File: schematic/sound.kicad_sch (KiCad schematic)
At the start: 14 parts, among them J2 Conn_01x02, U1 LM386, U2 SN76489AN

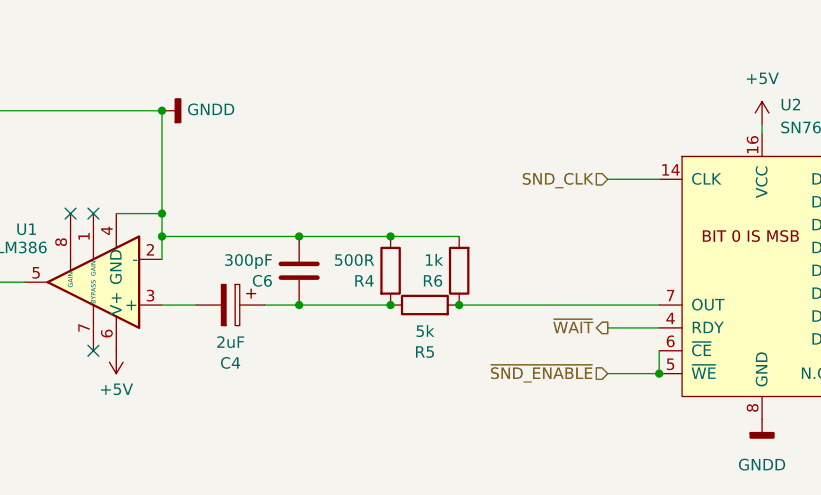
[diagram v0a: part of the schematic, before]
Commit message: added volume and adjusted cart port
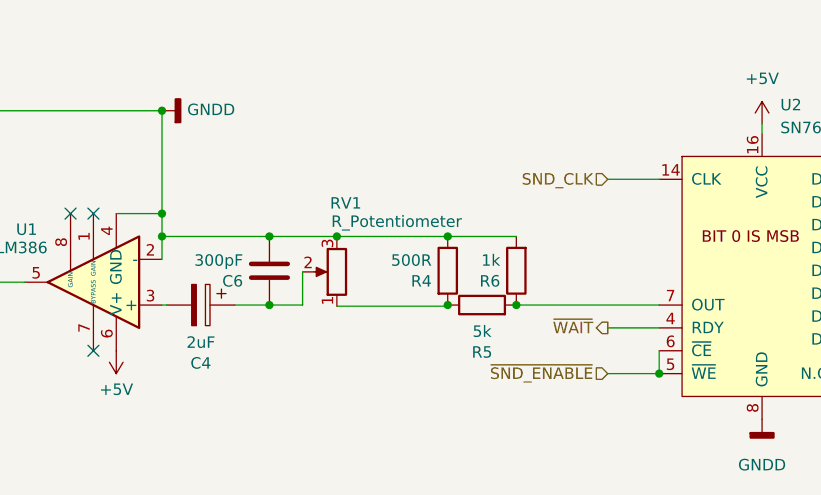
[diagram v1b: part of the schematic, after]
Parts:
- added RV1: R_Potentiometer, RV100F-30:RV100F304K1B50K, symbol Device:R_Potentiometer
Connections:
- net GNDD: now also RV1.3
- net at R4.2, R5.1: now also RV1.1; no longer C4.1, C6.2
- new net: C4.1, C6.2, RV1.2
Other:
- moved on the sheet: C4, C6, R4, R5, R6

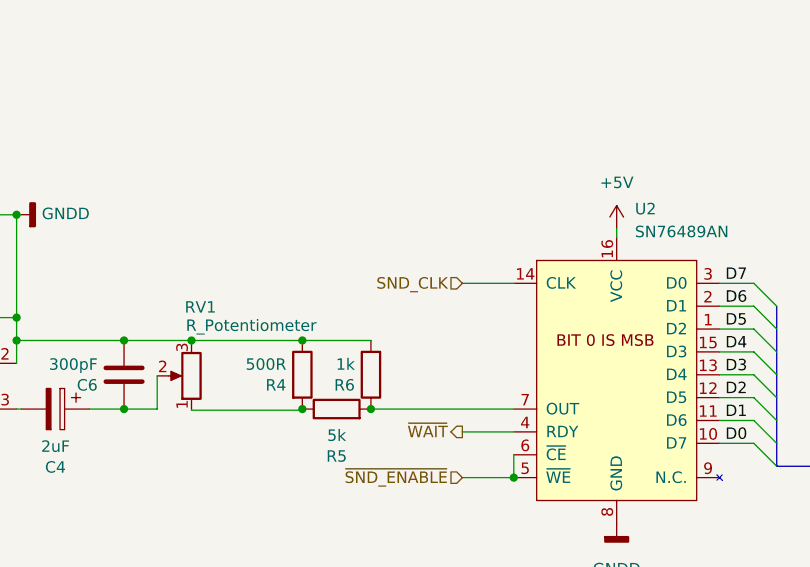
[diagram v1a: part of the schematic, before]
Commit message: added power port for lcd and adjusted board traces and fill
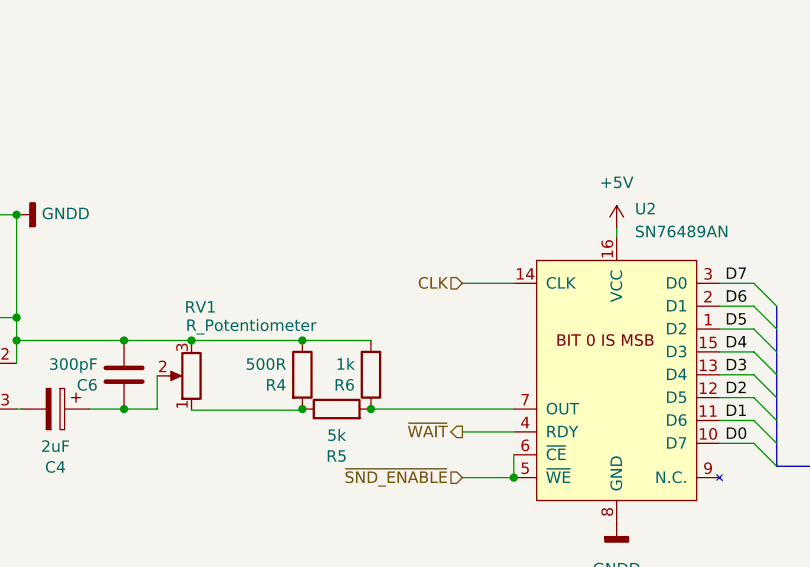
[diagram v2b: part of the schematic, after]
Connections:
- net SND_CLK renamed CLK
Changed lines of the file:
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@@
     (effects (font (size 1.27 1.27)) (justify right))
   )
-  (hierarchical_label "SND_CLK" (shape input) (at 169.291 95.25 180) (fields_autoplaced)
+  (hierarchical_label "CLK" (shape input) (at 169.291 95.25 180) (fields_autoplaced)
     (effects (font (size 1.27 1.27)) (justify right))
   )

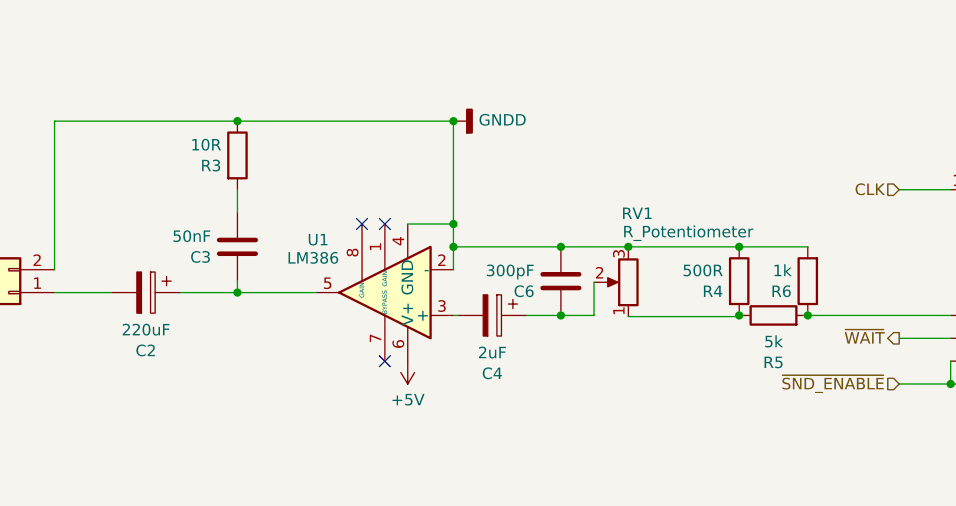
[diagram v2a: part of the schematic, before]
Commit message: first version with roller controller compat
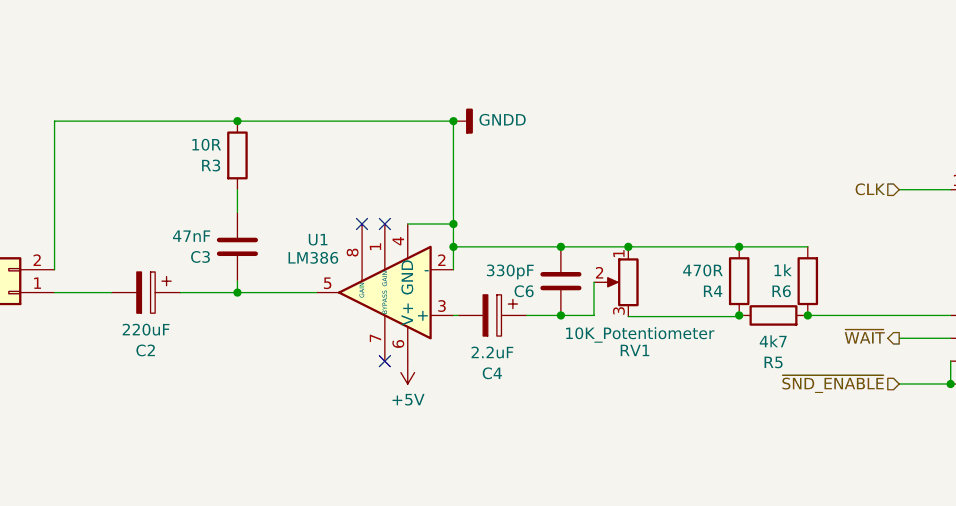
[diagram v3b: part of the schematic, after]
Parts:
- C3: value 50nF -> 47nF
- C4: value 2uF -> 2.2uF
- C6: value 300pF -> 330pF
- R4: value 500R -> 470R
- R5: value 5k -> 4k7
- RV1: value R_Potentiometer -> 10K_Potentiometer
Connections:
- net GNDD: now also RV1.1; no longer RV1.3
- net at R4.2, R5.1: now also RV1.3; no longer RV1.1
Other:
- moved on the sheet: RV1
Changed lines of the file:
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@@
       (effects (font (size 1.27 1.27)) (justify right))
     )
-    (property "Value" "500R" (at 149.733 104.267 0)
+    (property "Value" "470R" (at 149.733 104.267 0)
       (effects (font (size 1.27 1.27)) (justify right))
     )
@@
     )
   )
-  (symbol (lib_id "Device:R_Potentiometer") (at 139.192 105.537 180) (unit 1)
-    (in_bom yes) (on_board yes) (dnp no)
-    (property "Reference" "RV1" (at 138.43 97.917 0)
-      (effects (font (size 1.27 1.27)) (justify right))
-    )
-    (property "Value" "R_Potentiometer" (at 138.557 99.949 0)
+  (symbol (lib_id "Device:R_Potentiometer") (at 139.192 105.537 0) (mirror y) (unit 1)
+    (in_bom yes) (on_board yes) (dnp no)
+    (property "Reference" "RV1" (at 138.176 113.157 0)
+      (effects (font (size 1.27 1.27)) (justify right))
+    )
+    (property "Value" "10K_Potentiometer" (at 132.08 111.252 0)
       (effects (font (size 1.27 1.27)) (justify right))
     )
@@
       (effects (font (size 1.27 1.27)) (justify right))
     )
-    (property "Value" "300pF" (at 128.778 104.267 0)
+    (property "Value" "330pF" (at 128.778 104.267 0)
       (effects (font (size 1.27 1.27)) (justify right))
     )
@@
       (effects (font (size 1.27 1.27)))
     )
-    (property "Value" "5k" (at 155.321 112.1664 90)
+    (property "Value" "4k7" (at 155.321 112.1664 90)
       (effects (font (size 1.27 1.27)))
     )
@@
       (effects (font (size 1.27 1.27)) (justify right))
     )
-    (property "Value" "50nF" (at 92.837 100.457 0)
+    (property "Value" "47nF" (at 92.837 100.457 0)
       (effects (font (size 1.27 1.27)) (justify right))
     )
@@
       (effects (font (size 1.27 1.27)))
     )
-    (property "Value" "2uF" (at 124.079 113.3856 90)
-      (effects (font (size 1.27 1.27)))
-    )
+    (property "Value" "2.2uF" (at 124.079 113.3856 90)
+      (effects (font (size 1.27 1.27)))
+    )

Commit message: update pdf schematic and schematic wording
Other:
- title: Righteous Tentacle, Colecovision Reverse Engineering Project -> Mini Colecovision
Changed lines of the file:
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@@
   (paper "USLetter")
   (title_block
-    (title "Righteous Tentacle, Colecovision Reverse Engineering Project")
-    (date "2023-06-18")
-    (rev "1.0.0.F")
+    (title "Mini Colecovision")
+    (date "2024-03-25")
+    (rev "1.0.0")
     (company "sparkletron")
     (comment 1 "Jay Convertino")
     (comment 2 "MIT LICENSE")
-    (comment 3 "PCB: 75743 REV F")
+    (comment 3 "TARGET: Portable")
   )
   (junction (at 119.761 99.06) (diameter 0) (color 0 0 0 0)

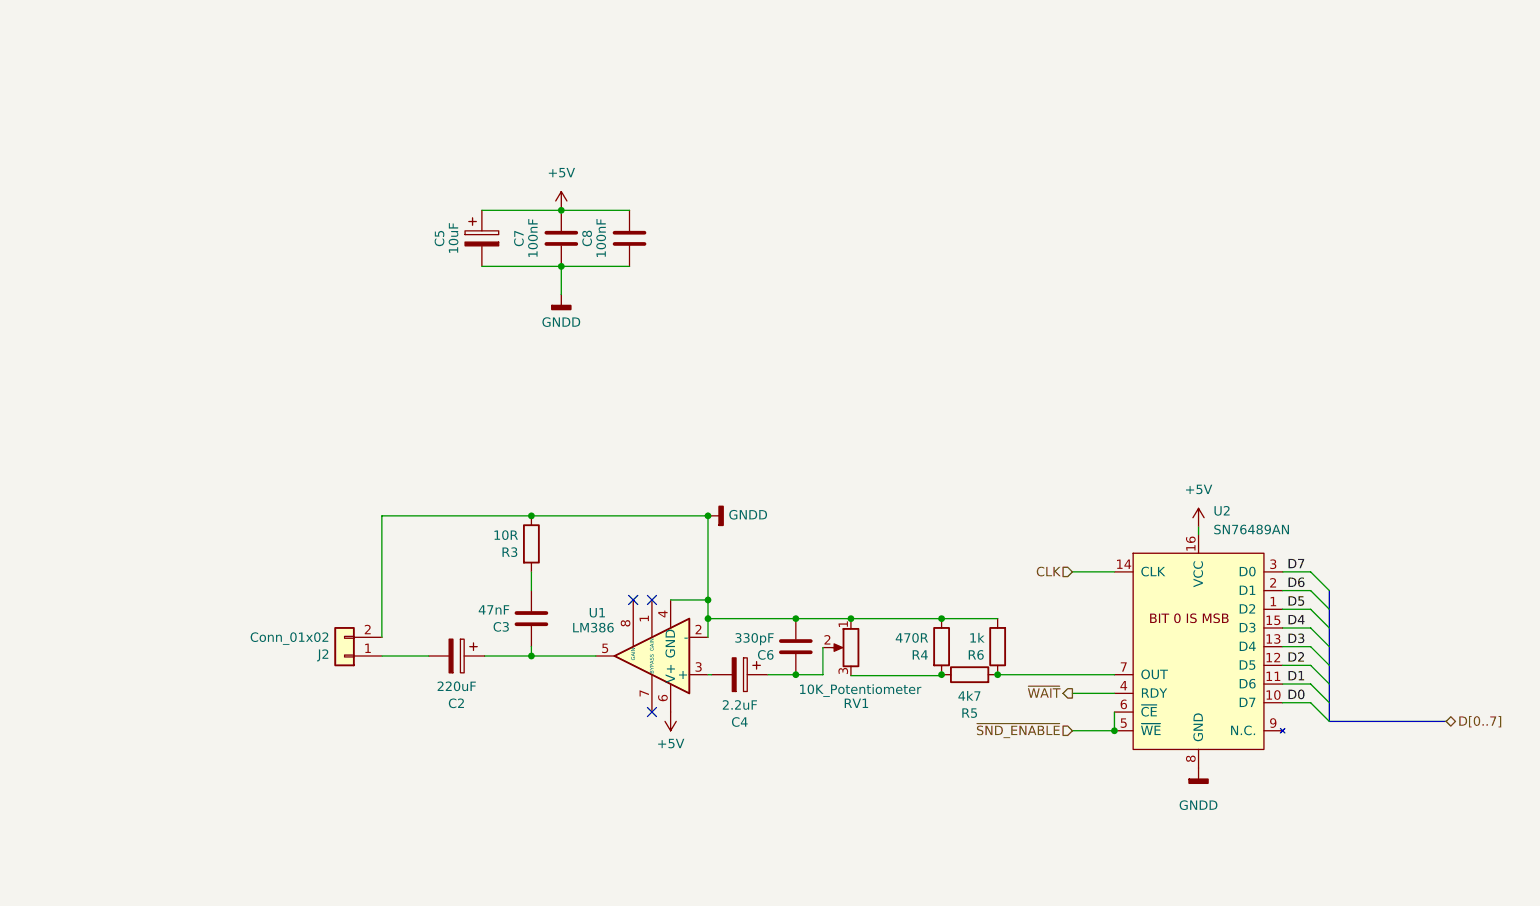
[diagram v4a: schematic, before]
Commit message: first commit with PCB revised for super game module. Needs model updates and tweaks
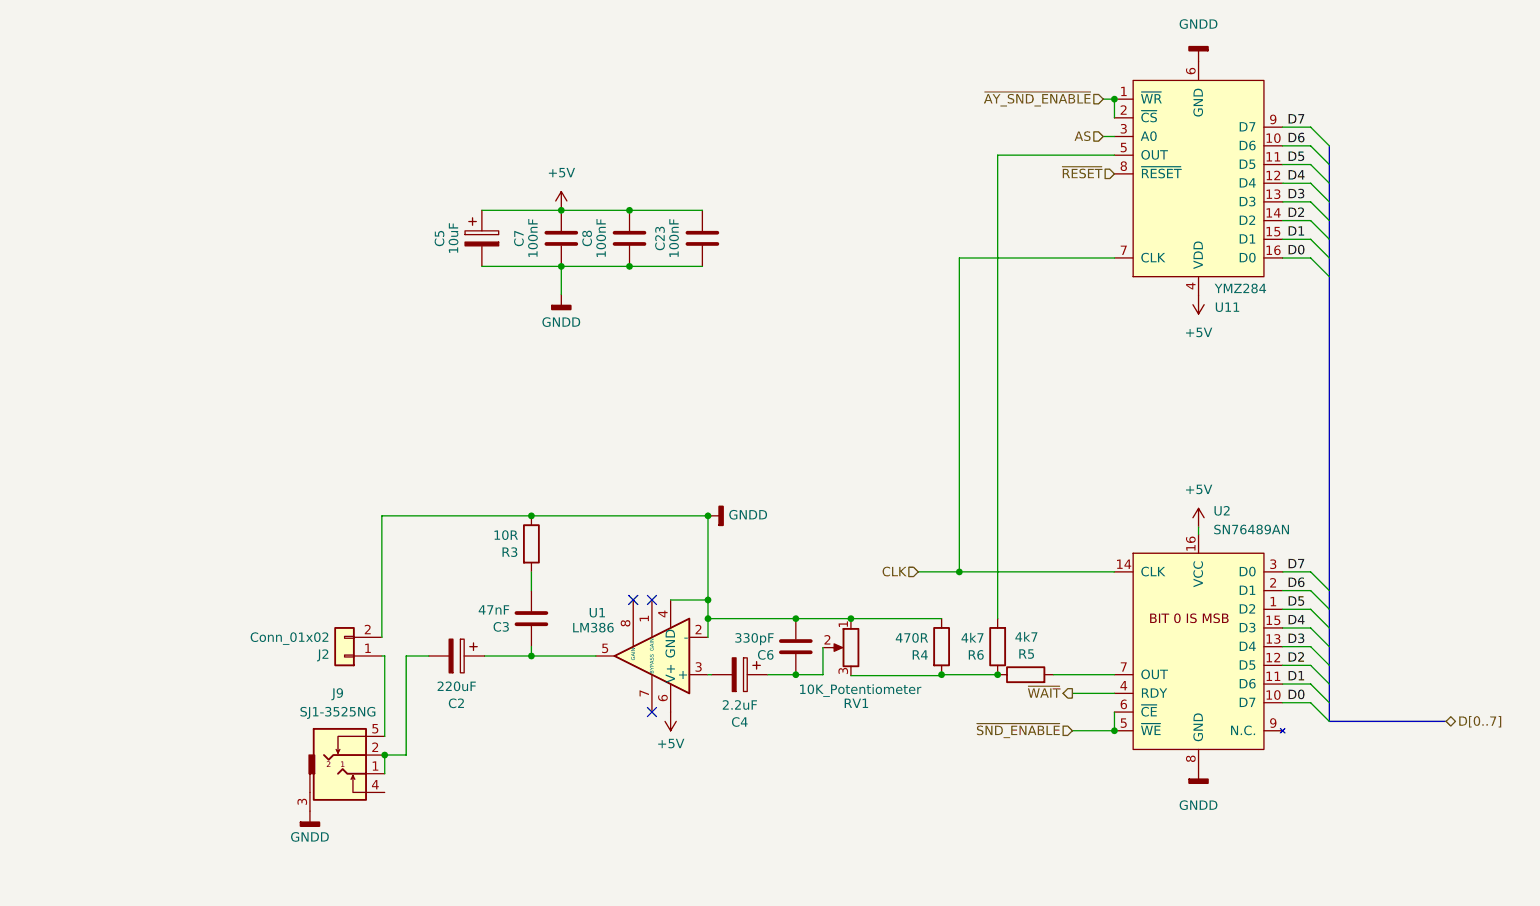
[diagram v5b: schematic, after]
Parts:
- added C23: 100nF, Capacitor_THT:C_Disc_D7.0mm_W2.5mm_P5.00mm, symbol Device:C
- added J9: SJ1-3525NG, jacks:spc21348, symbol jacks:eighth_inch_jack
- added U11: YMZ284, Package_DIP:DIP-16_W7.62mm, symbol Vintage_Audio_Synth:YMZ284
- R6: value 1k -> 4k7
- U1: footprint Package_DIP:DIP-8_W7.62mm_LongPads -> Package_DIP:DIP-8_W7.62mm
- U2: footprint Package_DIP:DIP-16_W7.62mm_LongPads -> Package_DIP:DIP-16_W7.62mm
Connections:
- net +5V: now also C23.1, U11.4 (VDD)
- net CLK: now also U11.7 (CLK)
- net D0: now also U11.16 (D0)
- net D1: now also U11.15 (D1)
- net D2: now also U11.14 (D2)
- net D3: now also U11.13 (D3)
- net D4: now also U11.12 (D4)
- net D5: now also U11.11 (D5)
- net D6: now also U11.10 (D6)
- net D7: now also U11.9 (D7)
- net GNDD: now also C23.2, J9.3, U11.6 (GND); no longer R6.2
- net at R4.2, R5.1, RV1.3: now also R6.1
- net at R5.2, U2.7 (OUT): no longer R6.1
- net at C2.2: now also J9.1, J9.2; no longer J2.1 (Pin_1)
- new net: J2.1 (Pin_1), J9.5
- new net: R6.2, U11.5 (OUT)
- new net AS: U11.3 (A0)
- new net ~{AY_SND_ENABLE}: U11.1 (~{WR}), U11.2 (~{CS})
- new net ~{RESET}: U11.8 (~{RESET})
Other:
- moved on the sheet: R5
